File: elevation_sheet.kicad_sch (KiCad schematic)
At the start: 16 parts, among them SW2 SW_SPDT_312, SW4 Right Limit Switch, SW5 Left Limit Switch, U2 74LS08, U3 ICM7555xP, U4 74LS32

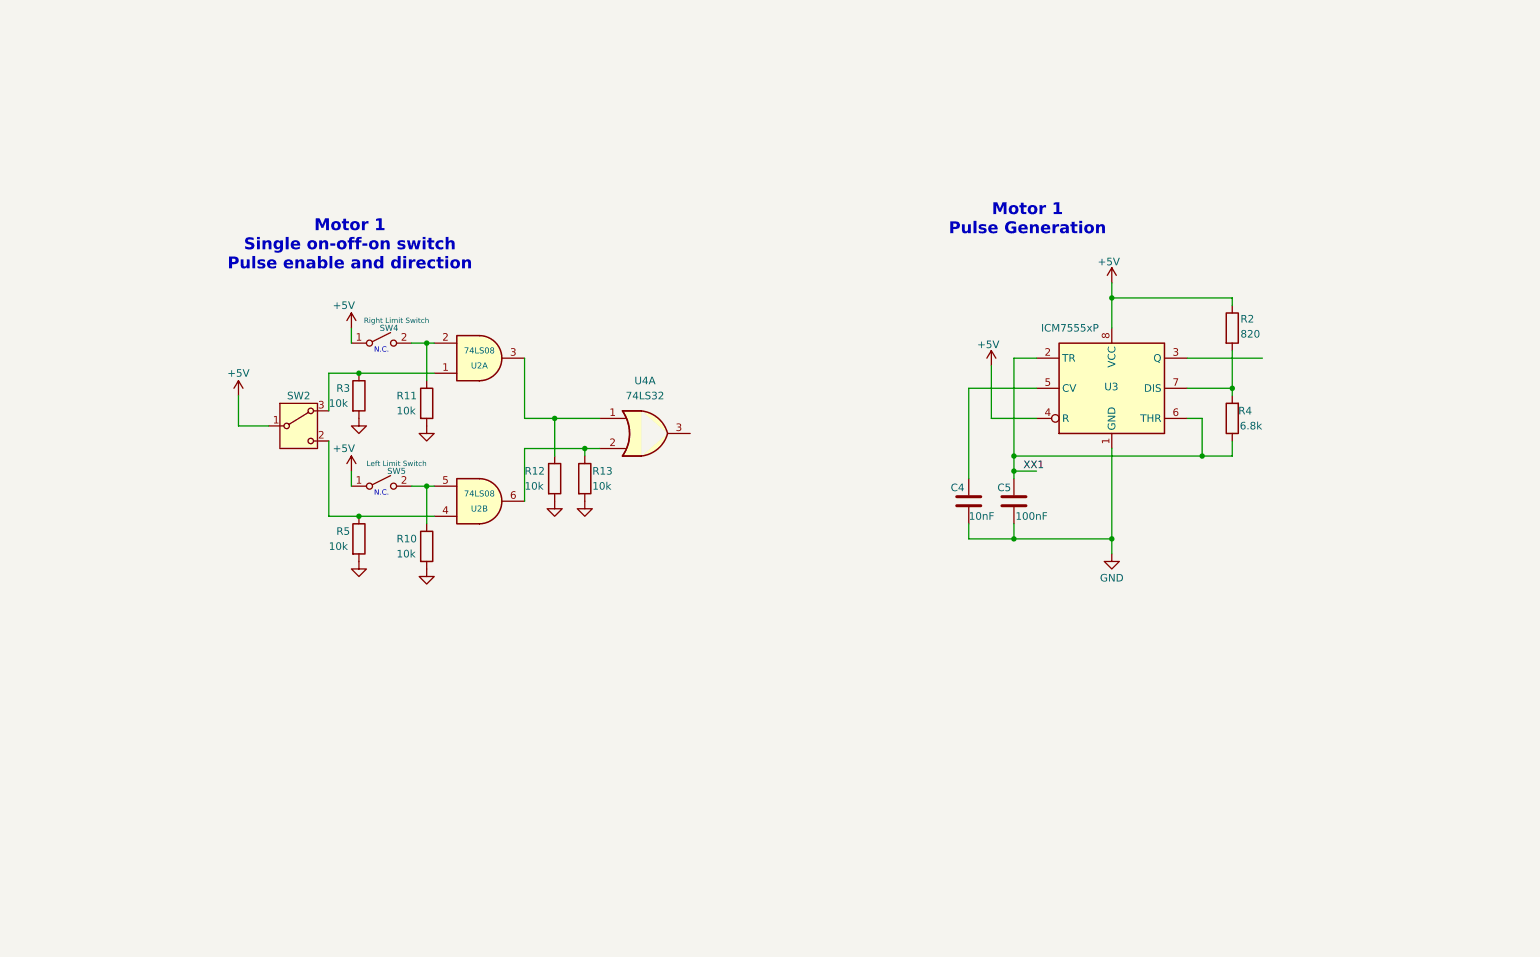
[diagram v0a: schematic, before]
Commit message: Elevation sheet mostly complete
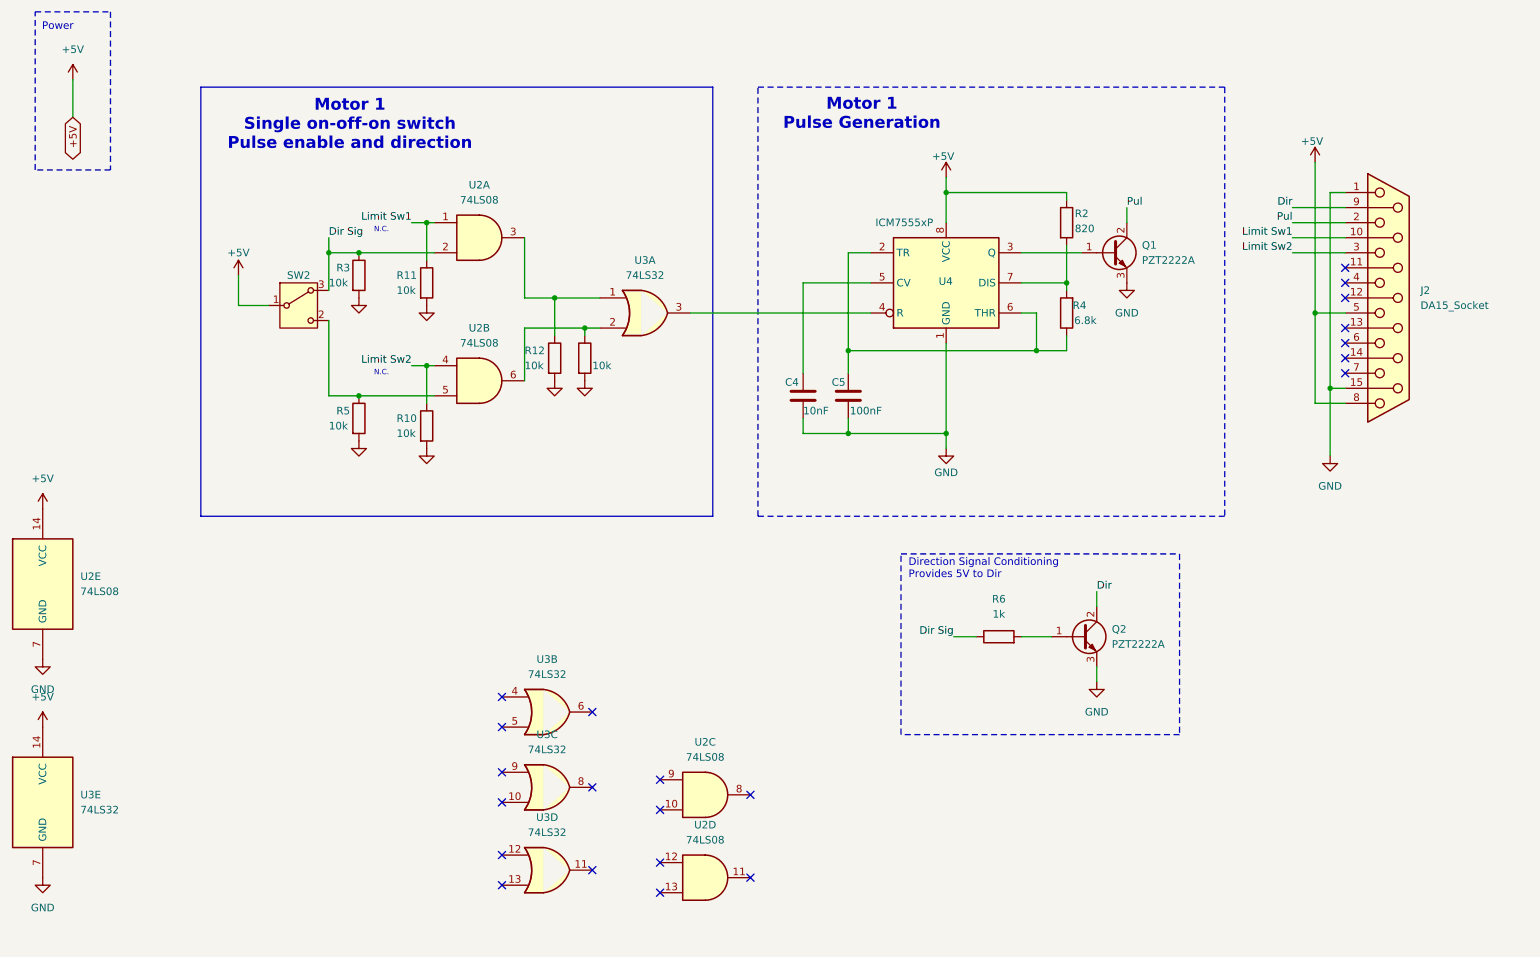
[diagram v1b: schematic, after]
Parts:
- removed SW4: Right Limit Switch, symbol Switch:SW_SPST
- removed SW5: Left Limit Switch, symbol Switch:SW_SPST
- removed U4: 74LS32, symbol 74xx:74LS32
- added J2: DA15_Socket, Connector_Dsub:DSUB-15_Socket_Horizontal_P2.77x2.54mm_EdgePinOffset9.40mm, symbol Connector:DA15_Socket
- added Q1, Q2: PZT2222A, Package_TO_SOT_SMD:SOT-223-3_TabPin2, symbol Transistor_BJT:PZT2222A
- added R6: 1k, symbol Device:R
- added unit 3 of U2
- added unit 5 of U2
- added unit 4 of U2
- added U3: 74LS32, symbol 74xx:74LS32
- renumbered U3 to U4
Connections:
- net +5V: now also J2.5, J2.8, U2.14 (VCC), U3.14 (VCC); no longer U4.4 (R)
- net GND: now also J2.1, J2.15 (P15), Q1.3 (E), Q2.3 (E), U2.7 (GND), U3.7 (GND)
- net at U2.5: now also R5.1, SW2.2 (C); no longer R10.1
- net Dir Sig: now reaches R3.1, SW2.3 (A)
- net Dir Sig: now also U2.2, R6.1; no longer U2.1
- net Limit Sw1: now reaches R11.1
- net Limit Sw1: now also U2.1, J2.10 (P10); no longer U2.2
- net at R12.1, U2.3: now also U3.1
- net at U4.3 (Q): now also Q1.1 (B)
- net at R13.1, U2.6: now also U3.2
- new net: U3.3, U4.4 (R)
- new net: Q2.1 (B), R6.2
- new net Dir: J2.9 (P9), Q2.2 (C)
- new net Limit Sw2: J2.3, R10.1, U2.4
- new net Pul: J2.2, Q1.2 (C)
- no-connect marks 0 -> 22
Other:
- note added: "Direction Signal Conditioning Provides 5V to Dir"
- note added: "Power"
- moved on the sheet: C4, C5, R10, R11, R12, R2, R3, R4, R5, SW2, U4

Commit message: Added Azimuth
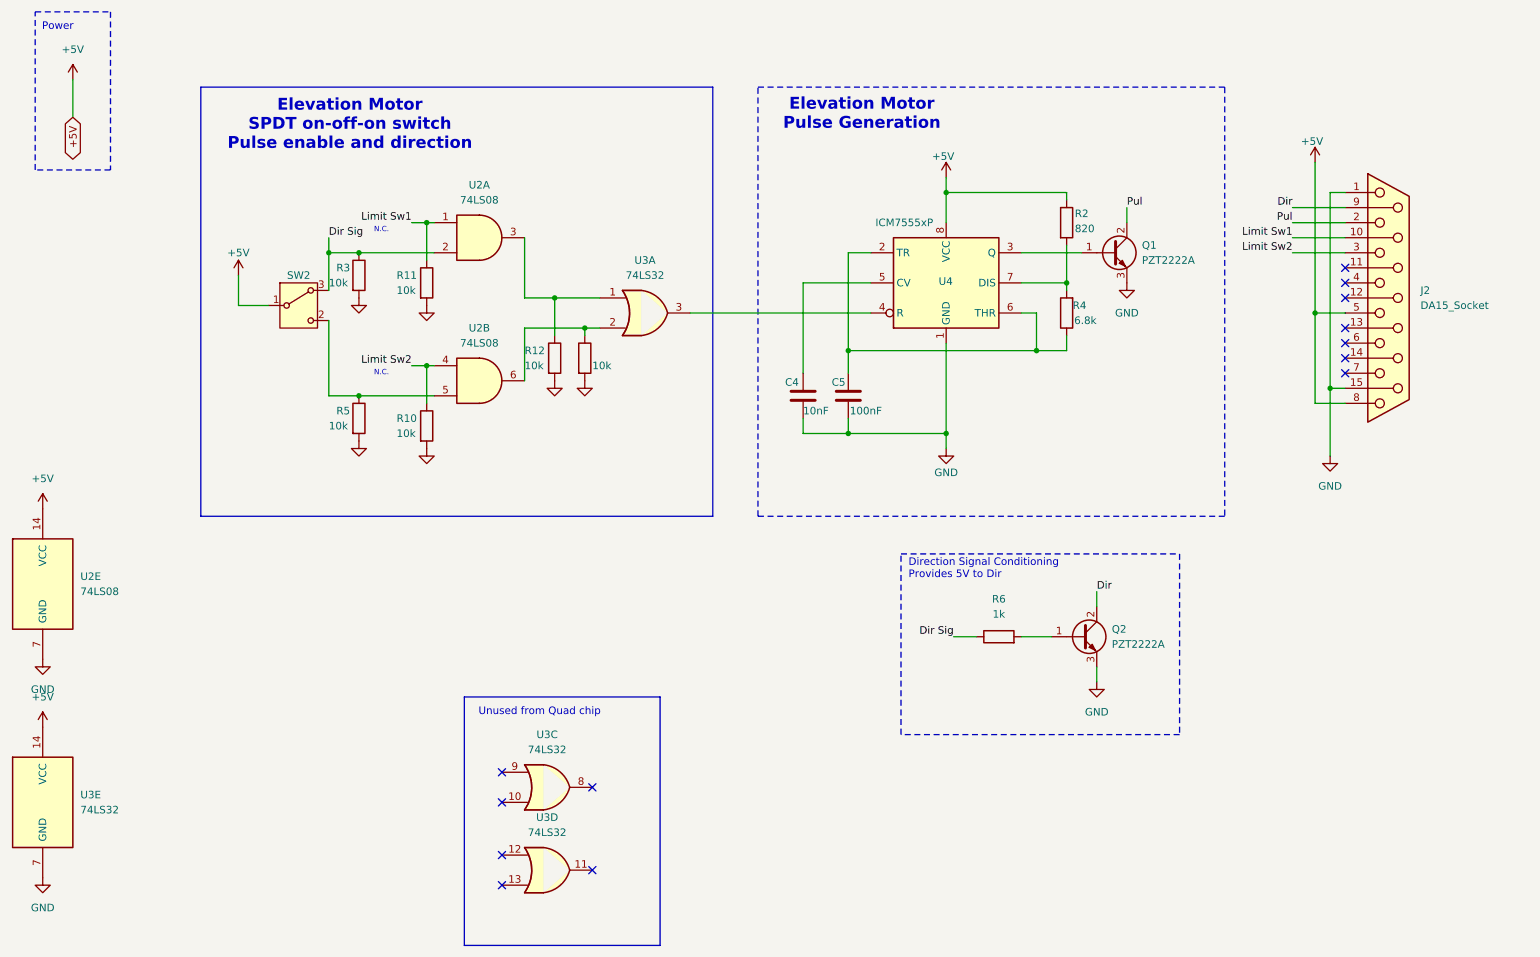
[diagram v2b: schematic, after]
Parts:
- removed unit 3 of U2
- removed unit 4 of U2
- removed unit 2 of U3
- U4: footprint Package_DIP:DIP-8_W7.62mm -> Package_SO:SOIC-8_3.9x4.9mm_P1.27mm; symbol Timer:ICM7555xP -> Timer:ICM7555xB
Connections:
- no-connect marks 22 -> 13
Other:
- note added: "Elevation Motor Pulse Generation"
- note added: "Elevation Motor SPDT on-off-on switch Pulse enable and direction"
- note added: "Unused from Quad chip"
- note removed: "Motor 1 Pulse Generation"
- note removed: "Motor 1 Single on-off-on switch Pulse enable and direction"

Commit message: Latest versions
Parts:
- added J4: CRJ022-G-TH, CRJ022-G-TH:CUI_CRJ022-G-TH, symbol CRJ022-G-TH:CRJ022-G-TH
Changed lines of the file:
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@@
+	)
+	(symbol
+		(lib_id "CRJ022-G-TH:CRJ022-G-TH")
+		(at 260.35 125.73 0)
+		(unit 1)
+		(exclude_from_sim no)
+		(in_bom yes)
+		(on_board yes)
+		(dnp no)
+		(fields_autoplaced yes)
+		(property "Reference" "J4"
+			(at 269.24 128.2699 0)
+			(effects
+				(font
+					(size 1.27 1.27)
+				)
+				(justify left)
+			)
+		)
+		(property "Value" "CRJ022-G-TH"
+			(at 269.24 130.8099 0)
+			(effects
+				(font
+					(size 1.27 1.27)
+				)
+				(justify left)
+			)
+		)
+		(property "Footprint" "CRJ022-G-TH:CUI_CRJ022-G-TH"
+			(at 260.35 125.73 0)
+			(effects
+				(font
+					(size 1.27 1.27)
+				)
+				(justify bottom)
+				(hide yes)
+			)
+		)
+		(property "Datasheet" ""
+			(at 260.35 125.73 0)
+			(effects
+				(font
+					(size 1.27 1.27)
+				)
+				(hide yes)
+			)
+		)
+		(property "Description" ""
+			(at 260.35 125.73 0)
+			(effects
+				(font
+					(size 1.27 1.27)
+				)
+				(hide yes)
+			)
+		)
+		(property "PARTREV" "1.0"
+			(at 260.35 125.73 0)
+			(effects
+				(font
+					(size 1.27 1.27)
+				)
+				(justify bottom)
+				(hide yes)
+			)
+		)
+		(property "STANDARD" "Manufacturer Recommendations"
+			(at 260.35 125.73 0)
+			(effects
+				(font
+					(size 1.27 1.27)
+				)
+				(justify bottom)
+				(hide yes)
+			)
+		)
+		(property "MAXIMUM_PACKAGE_HEIGHT" "14.05mm"
+			(at 260.35 125.73 0)
+			(effects
+				(font
+					(size 1.27 1.27)
+				)
+				(justify bottom)
+				(hide yes)
+			)
+		)
+		(property "MANUFACTURER" "CUI Devices"
+			(at 260.35 125.73 0)
+			(effects
+				(font
+					(size 1.27 1.27)
+				)
+				(justify bottom)
+				(hide yes)
+			)
+		)
+		(pin "6R"
+		)
+		(pin "8R"
+		)
+		(pin "7R"
+		)
+		(pin "7L"
+		)
+		(pin "3L"
+		)
+		(pin "1R"
+		)
+		(pin "4R"
+		)
+		(pin "1L"
+		)
+		(pin "5L"
+		)
+		(pin "6L"
+		)
+		(pin "2R"
+		)
+		(pin "5R"
+		)
+		(pin "2L"
+		)
+		(pin "S1"
+		)
+		(pin "4L"
+		)
+		(pin "S2"
+		)
+		(pin "S3"
+		)
+		(pin "3R"
+		)
+		(pin "8L"
+		)
+		(instances
+			(project ""
+				(path "/8648ccd3-30ce-4b98-baff-aeab56a7c9f5/a4809f50-064d-4cb7-b1f7-56bf09fb0ea4"
+					(reference "J4")
+					(unit 1)
+				)
+			)
+		)
 	)
 	(symbol
